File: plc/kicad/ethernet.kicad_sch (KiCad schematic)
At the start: 2 parts, among them U3 W5500

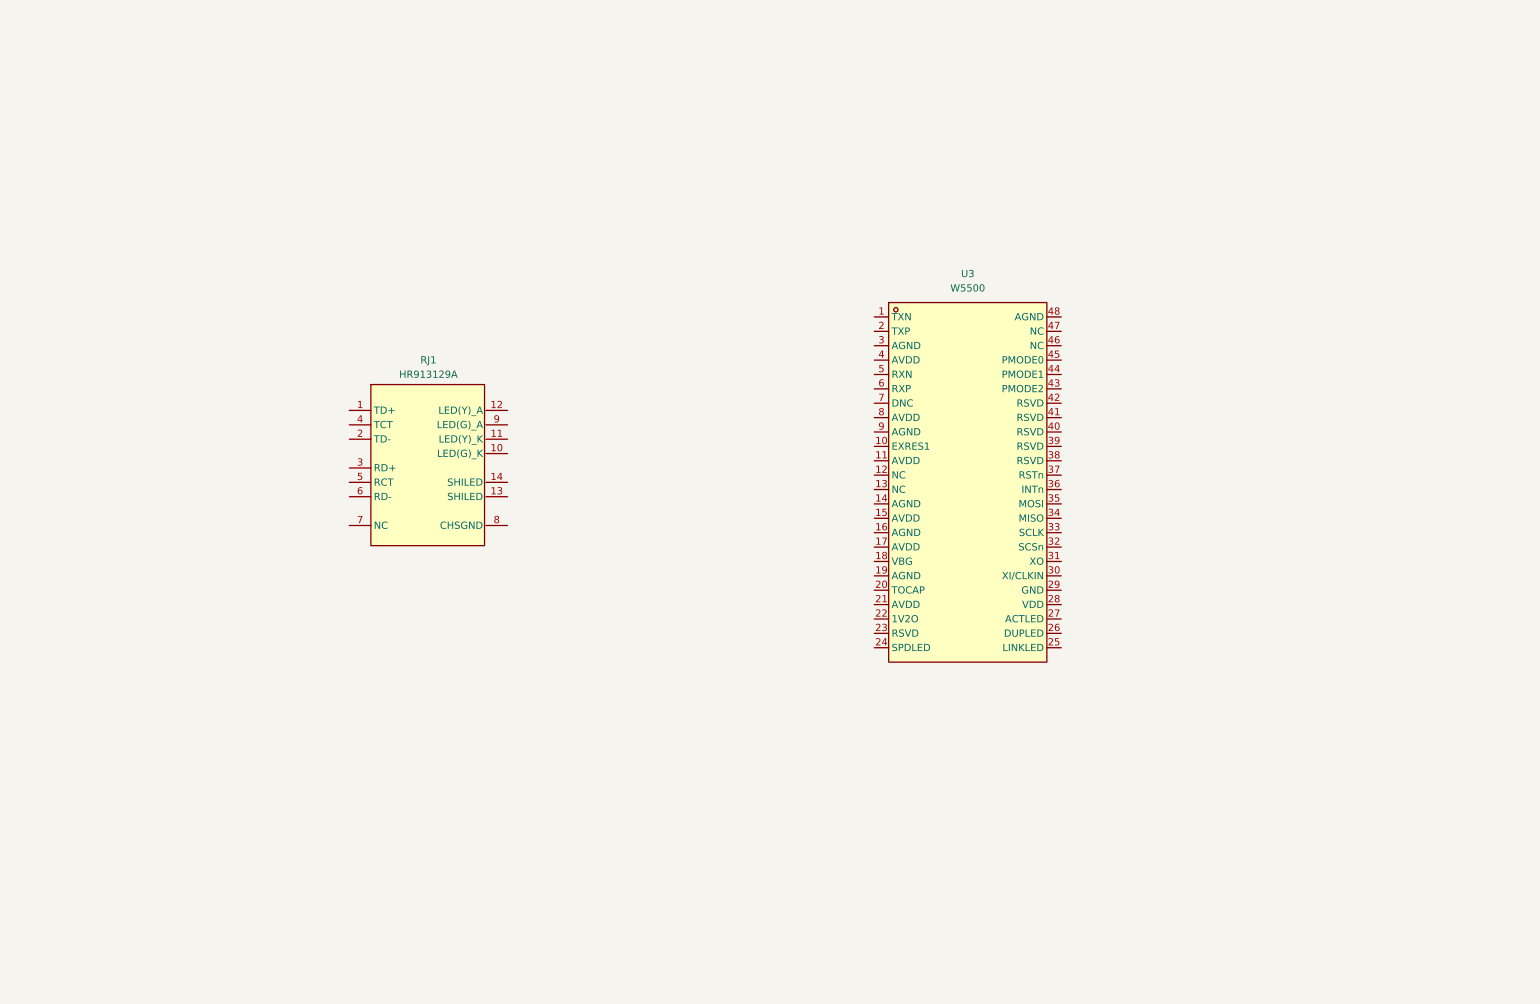
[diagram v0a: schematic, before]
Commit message: Updated ethernet circuit
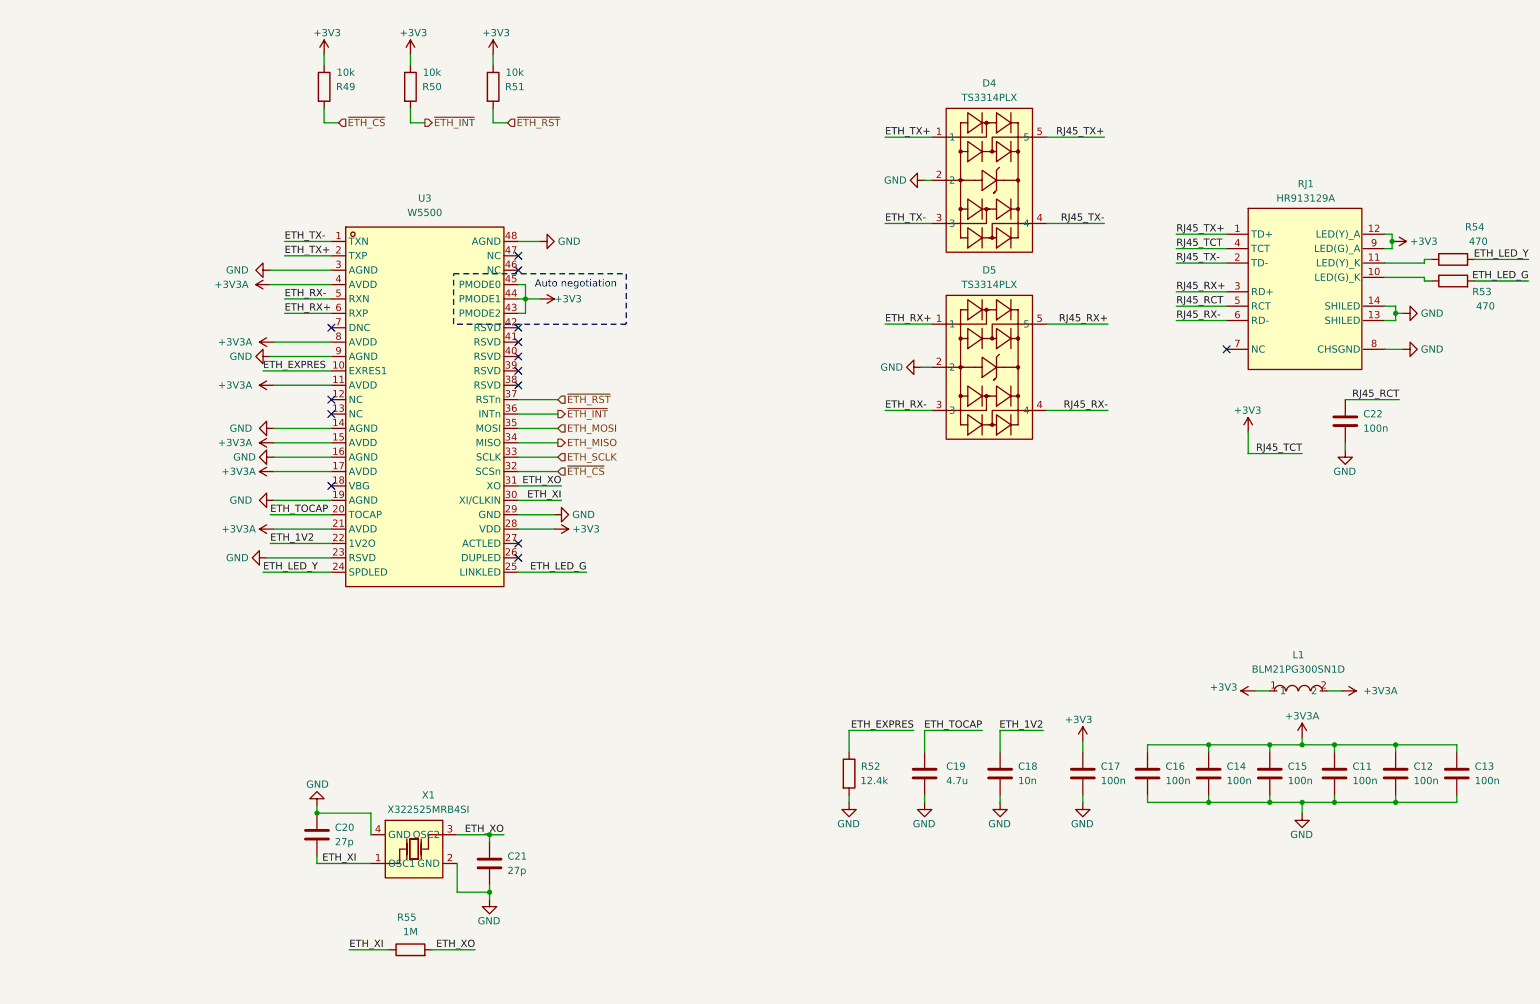
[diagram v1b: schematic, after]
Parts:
- added C11, C12, C13, C14, C15, C16, C17, C22: 100n, Capacitor_SMD:C_0805_2012Metric, symbol Device:C
- added C18: 10n, Capacitor_SMD:C_0805_2012Metric, symbol Device:C
- added C19: 4.7u, Capacitor_SMD:C_0805_2012Metric, symbol Device:C
- added C20, C21: 27p, Capacitor_SMD:C_0805_2012Metric, symbol Device:C
- added D4, D5: TS3314PLX, LibrePLC32:SOT-23-5_L2.9-W1.6-P0.95-LS2.8-BR, symbol LibrePLC32:TS3314PLX
- added L1: BLM21PG300SN1D, LibrePLC32:L0805, symbol LibrePLC32:BLM21PG300SN1D
- added R49, R50, R51: 10k, Resistor_SMD:R_0805_2012Metric, symbol Device:R
- added R52: 12.4k, Resistor_SMD:R_0805_2012Metric, symbol Device:R
- added R53, R54: 470, Resistor_SMD:R_0805_2012Metric, symbol Device:R
- added R55: 1M, Resistor_SMD:R_0805_2012Metric, symbol Device:R
- added X1: X322525MRB4SI, LibrePLC32:OSC-SMD_4P-L3.2-W2.5-BL_SIT8008BI, symbol LibrePLC32:X322525MRB4SI
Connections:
- net RJ45_TX+: now reaches RJ1.1 (TD+)
- net RJ45_TX+: now also D4.5
- net at RJ1.10 (LED(G)_K): now also R53.1
- net at RJ1.11 (LED(Y)_K): now also R54.1
- net +3V3: now reaches RJ1.12 (LED(Y)_A)
- net +3V3: now also RJ1.4 (TCT), RJ1.9 (LED(G)_A), U3.28 (VDD), U3.43 (PMODE2), U3.44 (PMODE1), U3.45 (PMODE0), C17.1, L1.1, R49.1, R50.1, R51.1
- net GND: now reaches RJ1.13 (SHILED)
- net GND: now also RJ1.14 (SHILED), RJ1.8 (CHSGND), U3.14 (AGND), U3.16 (AGND), U3.19 (AGND), U3.23 (RSVD), U3.29 (GND), U3.3 (AGND), U3.48 (AGND), U3.9 (AGND), C11.2, C12.2, C13.2, C14.2, C15.2, C16.2, C17.2, C18.2, C19.2, C20.1, C21.2, C22.2, D4.2, D5.2, R52.2, X1.2 (GND), X1.4 (GND)
- net RJ45_TX-: now reaches RJ1.2 (TD-)
- net RJ45_TX-: now also D4.4
- net RJ45_RX+: now reaches RJ1.3 (RD+)
- net RJ45_RX+: now also D5.5
- net RJ45_RCT: now reaches RJ1.5 (RCT)
- net RJ45_RCT: now also C22.1
- net RJ45_RX-: now reaches RJ1.6 (RD-)
- net RJ45_RX-: now also D5.4
- net ETH_TX-: now reaches U3.1 (TXN)
- net ETH_TX-: now also D4.3
- net ETH_EXPRES: now reaches U3.10 (EXRES1)
- net ETH_EXPRES: now also R52.1
- net +3V3A: now reaches U3.11 (AVDD)
- net +3V3A: now also U3.15 (AVDD), U3.17 (AVDD), U3.21 (AVDD), U3.4 (AVDD), U3.8 (AVDD), C11.1, C12.1, C13.1, C14.1, C15.1, C16.1, L1.2
- net ETH_TX+: now reaches U3.2 (TXP)
- net ETH_TX+: now also D4.1
- net ETH_TOCAP: now reaches U3.20 (TOCAP)
- net ETH_TOCAP: now also C19.1
- net ETH_1V2: now reaches U3.22 (1V2O)
- net ETH_1V2: now also C18.1
- net ETH_LED_Y: now reaches U3.24 (SPDLED)
- net ETH_LED_Y: now also R54.2
- net ETH_LED_G: now reaches U3.25 (LINKLED)
- net ETH_LED_G: now also R53.2
- net ETH_XI: now reaches U3.30 (XI/CLKIN)
- net ETH_XI: now also C20.2, R55.1, X1.1 (OSC1)
- net ETH_XO: now reaches U3.31 (XO)
- net ETH_XO: now also C21.1, R55.2, X1.3 (OSC2)
- net ~{ETH_CS}: now reaches U3.32 (SCSn)
- net ~{ETH_CS}: now also R49.2
- net ETH_SCLK: now reaches U3.33 (SCLK)
- net ETH_MISO: now reaches U3.34 (MISO)
- net ETH_MOSI: now reaches U3.35 (MOSI)
- net ~{ETH_INT}: now reaches U3.36 (INTn)
- net ~{ETH_INT}: now also R50.2
- net ~{ETH_RST}: now reaches U3.37 (RSTn)
- net ~{ETH_RST}: now also R51.2
- net ETH_RX-: now reaches U3.5 (RXN)
- net ETH_RX-: now also D5.3
- net ETH_RX+: now reaches U3.6 (RXP)
- net ETH_RX+: now also D5.1
- no-connect marks 0 -> 14
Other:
- note added: "Auto negotiation"
- moved on the sheet: RJ1, U3

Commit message: Added netclasses
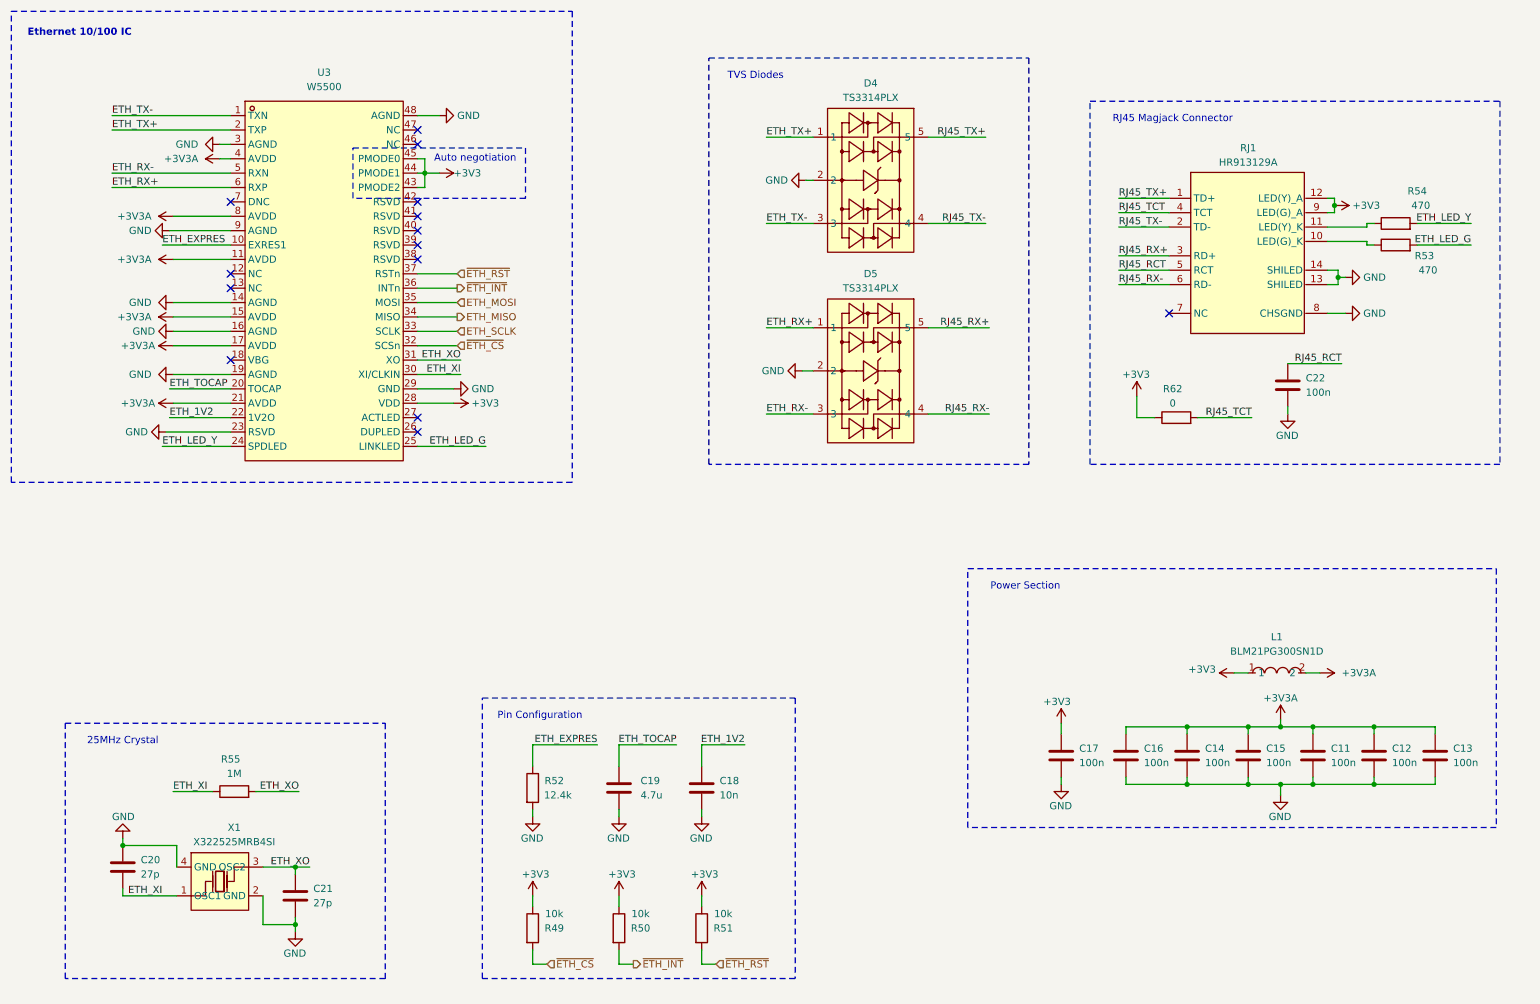
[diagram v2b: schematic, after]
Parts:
- added R62: 0, Resistor_SMD:R_0805_2012Metric, symbol Device:R
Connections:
- net +3V3: now also R62.1; no longer RJ1.4 (TCT)
- new net RJ45_TCT: R62.2, RJ1.4 (TCT)
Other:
- note added: "25MHz Crystal"
- note added: "Ethernet 10/100 IC"
- note added: "Pin Configuration"
- note added: "Power Section"
- note added: "RJ45 Magjack Connector"
- note added: "TVS Diodes"
- moved on the sheet: C11, C12, C13, C14, C15, C16, C17, C18, C19, C20, C21, C22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

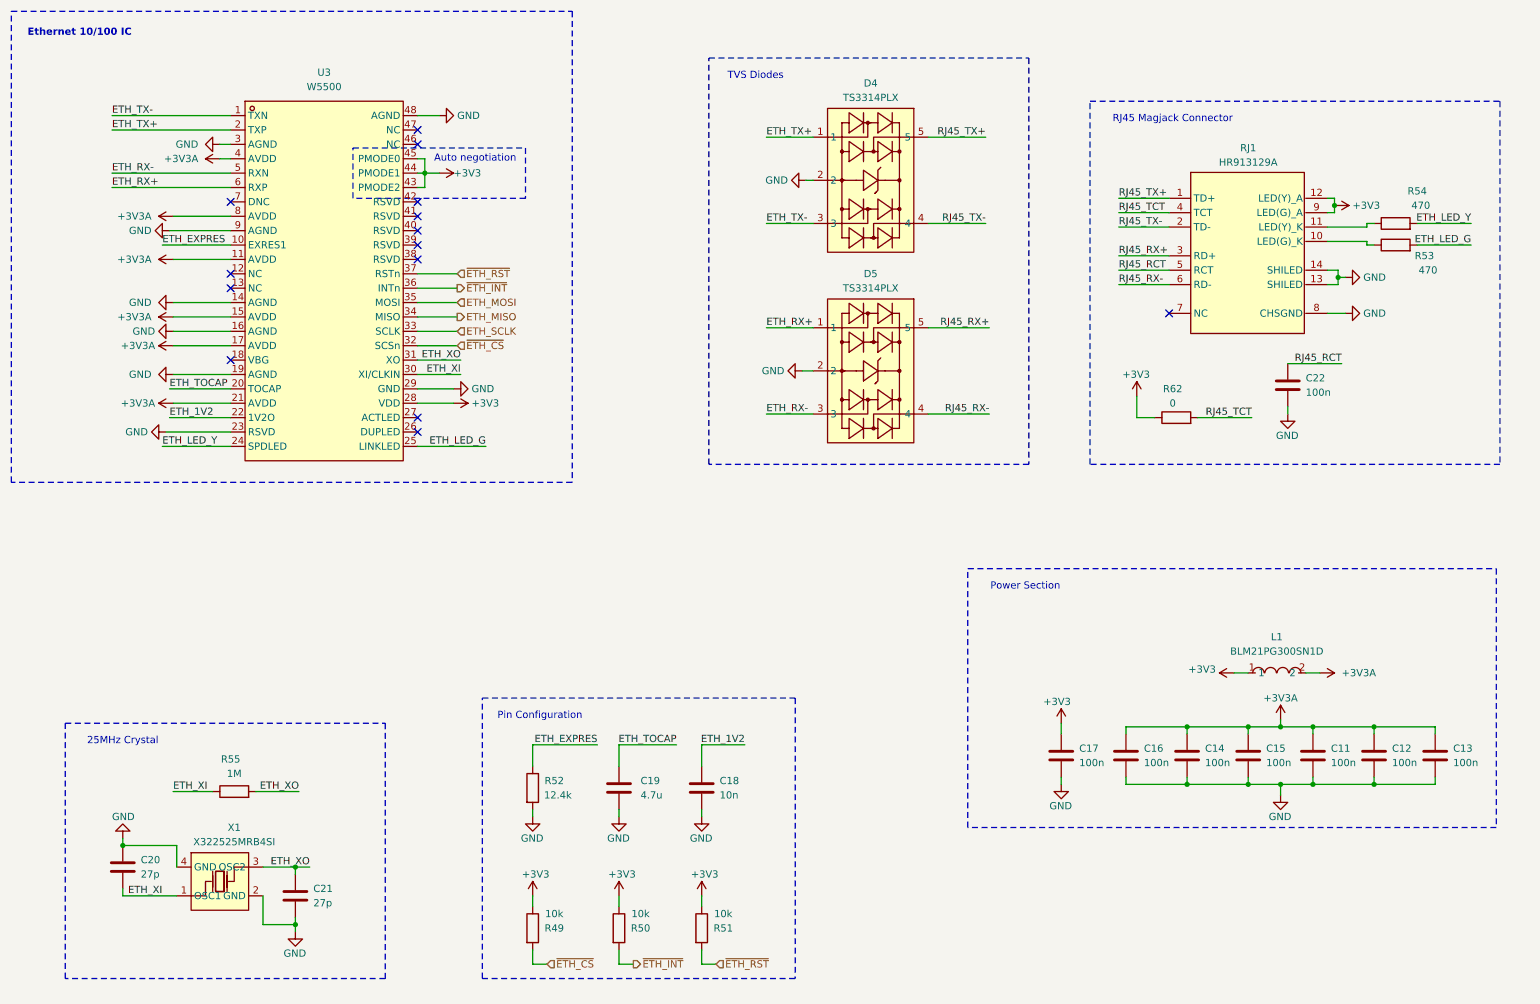
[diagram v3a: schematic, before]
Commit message: Added CP2102N bridge
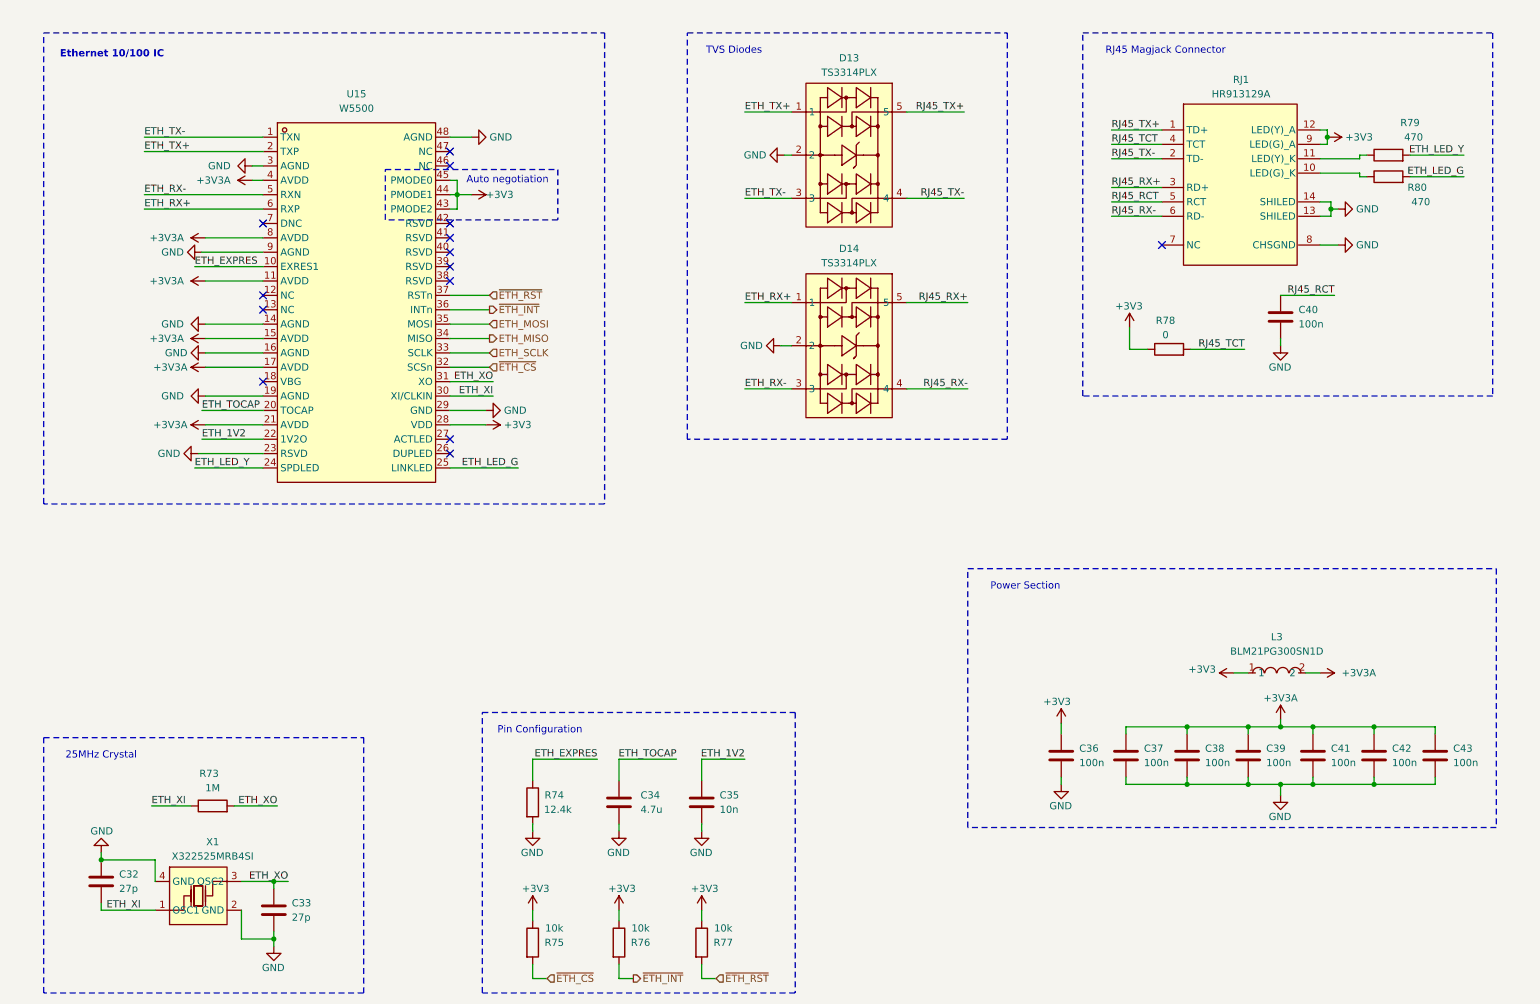
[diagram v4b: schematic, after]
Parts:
- renumbered C20 to C32, C21 to C33, C19 to C34, C18 to C35, C17 to C36, C16 to C37, C14 to C38, C15 to C39, C22 to C40, C11 to C41, C12 to C42, C13 to C43, D4 to D13, D5 to D14, L1 to L3, R55 to R73, R52 to R74, R49 to R75, R50 to R76, R51 to R77, R62 to R78, R54 to R79, R53 to R80, U3 to U15
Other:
- moved on the sheet: C32, C33, C34, C35, C40, D13, D14, R73, R74, R75, R76, R77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

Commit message: Added 3.3V regulator
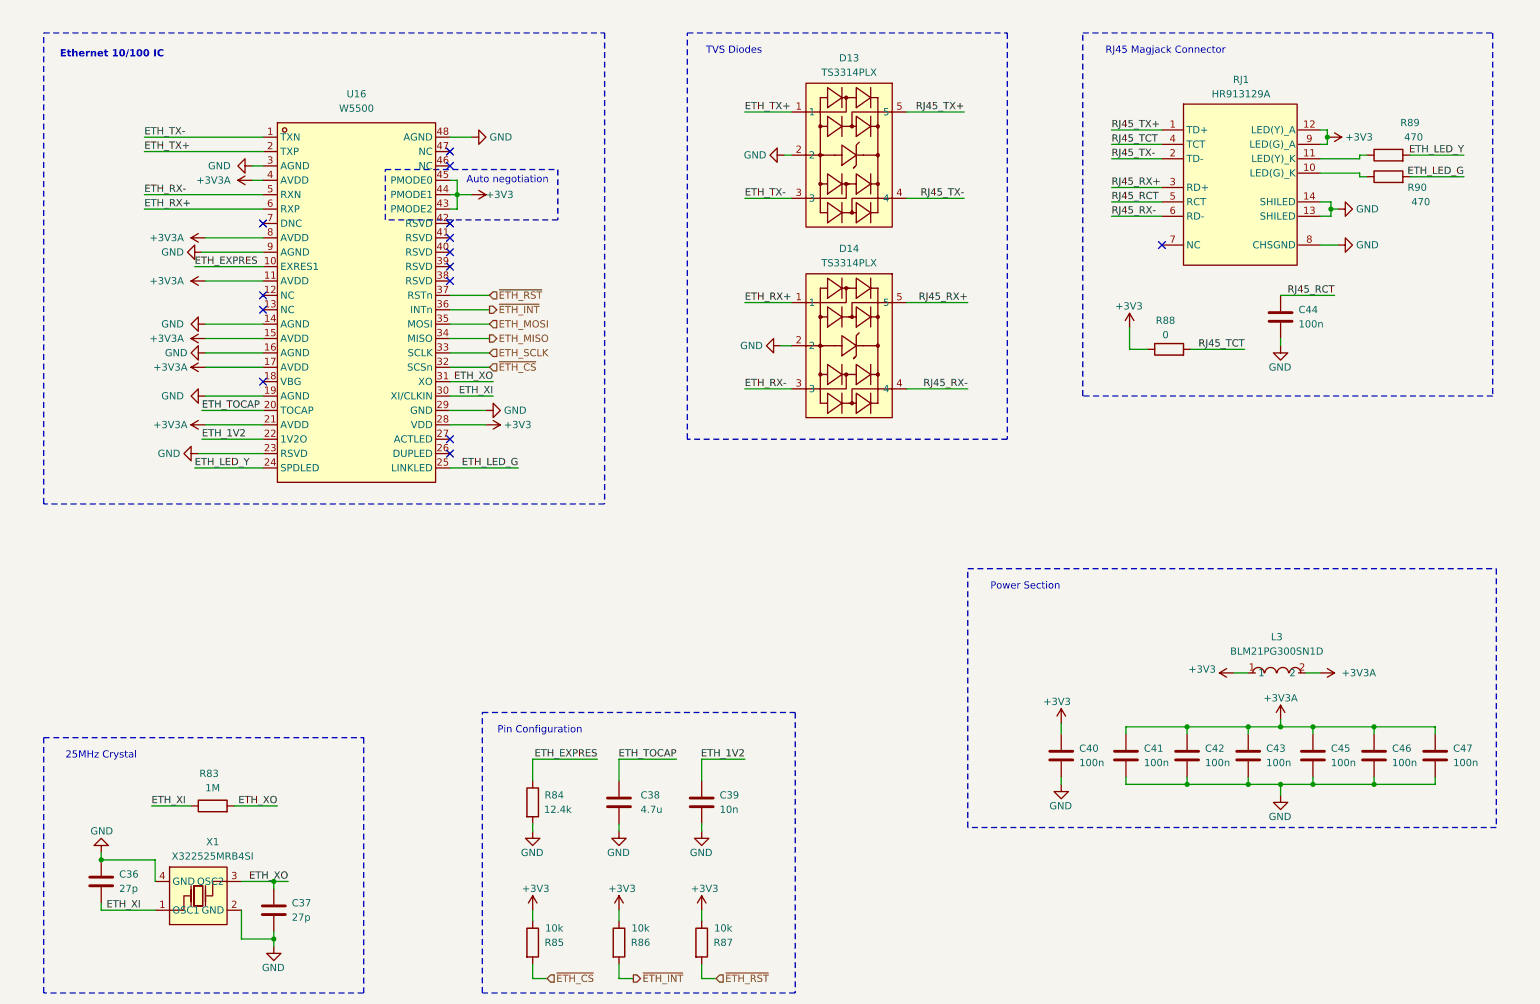
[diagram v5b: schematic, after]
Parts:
- renumbered C32 to C36, C33 to C37, C34 to C38, C35 to C39, C36 to C40, C37 to C41, C38 to C42, C39 to C43, C40 to C44, C41 to C45, C42 to C46, C43 to C47, R73 to R83, R74 to R84, R75 to R85, R76 to R86, R77 to R87, R78 to R88, R79 to R89, R80 to R90, U15 to U16
